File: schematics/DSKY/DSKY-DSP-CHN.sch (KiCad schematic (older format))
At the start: 5 parts, among them U20 74LS273, U21 74LS273, U22 74LS273, U5 74LS04, U7 74LS08

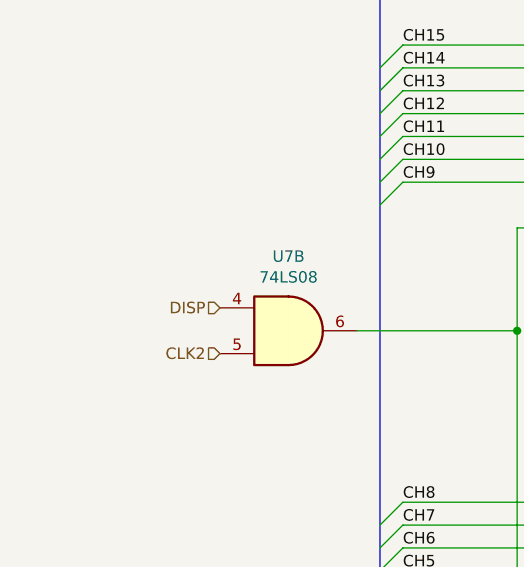
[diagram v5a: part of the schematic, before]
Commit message: Overhauled the handling of the sign characters.
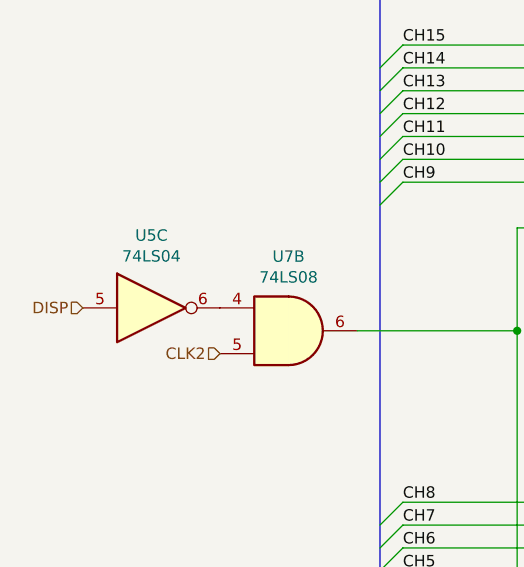
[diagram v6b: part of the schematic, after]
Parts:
- added unit 3 of U5
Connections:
- net DISP: now also U5.5; no longer U7.4
- new net: U5.6, U7.4
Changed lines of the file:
@@
 	1    0    0    -1
 $EndComp
-Text HLabel 2800 4600 0    50   Input ~ 0
+Text HLabel 2200 4600 0    50   Input ~ 0
 DISP
 Text HLabel 8150 2350 0    50   Input ~ 0
@@
 Wire Bus Line
 	3500 3100 3500 6300
+$Comp
+L 74xx:74LS04 U5
+U 3 1 6221121E
+P 2500 4600
+F 0 "U5" H 2500 4917 50  0000 C CNN
+F 1 "74LS04" H 2500 4826 50  0000 C CNN
+F 2 "" H 2500 4600 50  0001 C CNN
+F 3 "http://www.ti.com/lit/gpn/sn74LS04" H 2500 4600 50  0001 C CNN
+	3    2500 4600
+	1    0    0    -1
+$EndComp
 $EndSCHEMATC
